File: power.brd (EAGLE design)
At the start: 90.2 x 95.9 mm, 19 parts, among them J1 POWER_JACKPTH_BREAD, U1 LT3652

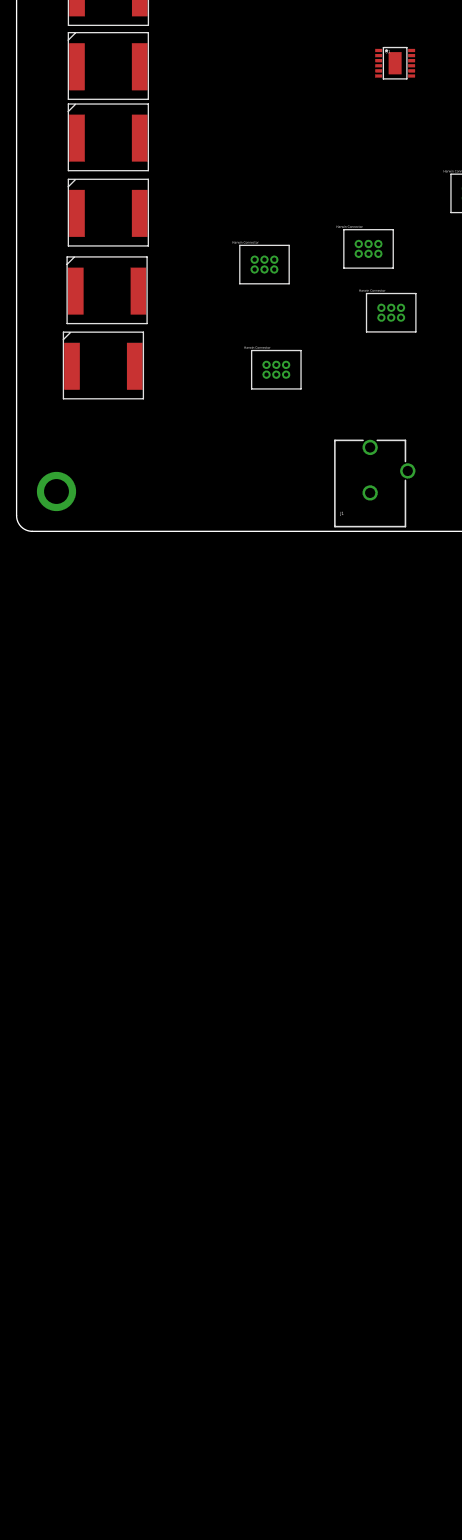
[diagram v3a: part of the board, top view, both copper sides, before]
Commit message: Added LT3688 dual regulator
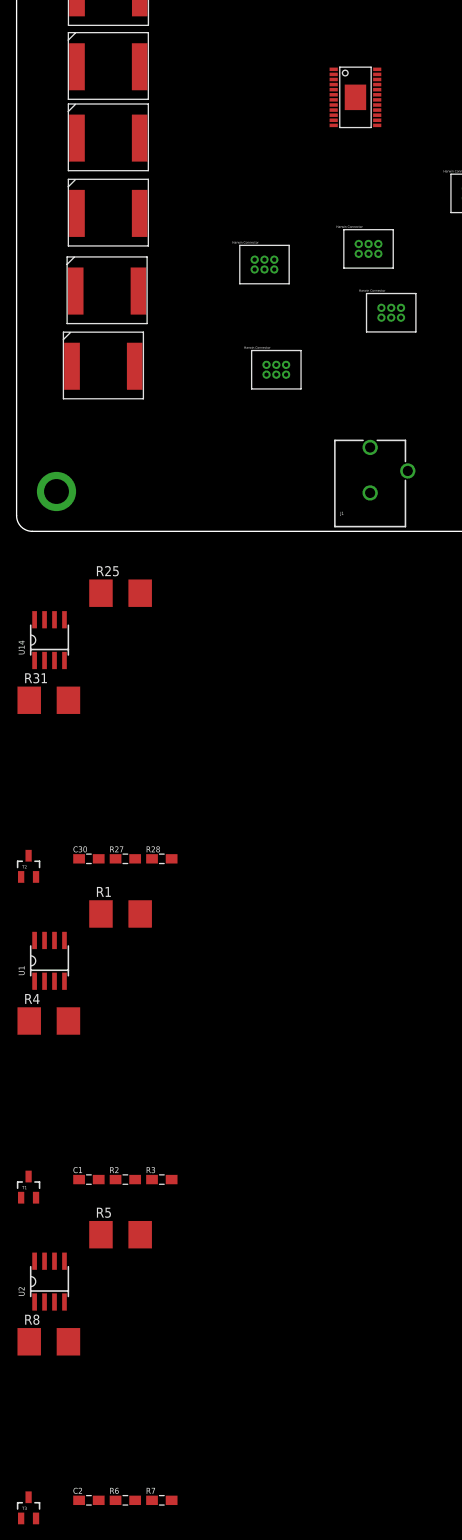
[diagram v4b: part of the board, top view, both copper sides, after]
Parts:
- added C1, C2, C30: .1uF, phonesat:0805
- added R1, R25, R31, R4, R5, R8: 0R, phonesat:2512
- added R2, R27, R6: 3K3, phonesat:0805
- added R28, R3, R7: 10K, phonesat:0805
- added T1, T2, T3: SINGLE_NCHAN_FET, phonesat:SOT23-3
- added U$13: LT3688, LT3688:LT3688TSSOP
- added U14, U2: MOSFET_PCHAN_20A, phonesat:SO8
- U1: value LT3652 -> MOSFET_PCHAN_20A; device SparkFun-PowerIC:MSOP-12_GND -> phonesat:SO8
- moved U1 122.7 mm to (4.20, -54.8)
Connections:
- new net ENAB_BURN1: R28.1, R3.1, R7.1
- new net N$1: R1.2, R4.2, U1.1, U1.2, U1.3
- new net N$19: R25.2, R31.2, U14.1, U14.2, U14.3
- new net N$2: C1.1, R3.2, T1.1
- new net N$21: C30.1, R28.2, T2.1
- new net N$24: R27.1, T2.3, U14.4
- new net N$3: R2.1, T1.3, U1.4
- new net N$4: R5.2, R8.2, U2.1, U2.2, U2.3
- new net N$5: C2.1, R7.2, T3.1
- new net N$6: R6.1, T3.3, U2.4
- new net VBURN1: U14.5, U14.6, U14.7, U14.8
- new net VBURN2: U1.5, U1.6, U1.7, U1.8
- new net VCC_8: R1.1, R2.2, R25.1, R27.2, R31.1, R4.1, R5.1, R6.2, R8.1
- new net VSOLAR: U$5.P3, U$5.P6
- net GND: now also C1.2, C2.2, C30.2, T1.2, T2.2, T3.2, U$1.P1, U$1.P4, U$2.P1, U$2.P4, U$3.P1, U$3.P4, U$4.P1, U$4.P4, U$5.P1, U$5.P4, U$6.P1, U$6.P4; no longer U1.13
- net VBURN3: now also U2.5, U2.6, U2.7, U2.8

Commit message: More switching regulator work
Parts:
- added C3, C4, C5: 0.22uF, SparkFun-Capacitors:0805
- added C31, C32: .1uF, phonesat:0805
- added C6, C7: 10pF, SparkFun-Capacitors:0805
- added C8, C9: 1nF, SparkFun-Capacitors:0805
- added R11: 523k, SparkFun-Resistors:0805
- added R12, R14: 100k, SparkFun-Resistors:0805
- added R13: 316k, SparkFun-Resistors:0805
- added R9: 10k, SparkFun-Resistors:0805
- C1: value .1uF -> 4.7uF; device phonesat:0805 -> SparkFun-Capacitors:0805
- C2: value .1uF -> 0.22uF; device phonesat:0805 -> SparkFun-Capacitors:0805
- moved C1 43.5 mm to (-1.42, -124.8)
- moved C2 16.6 mm to (-7.32, -124.8)
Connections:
- new net N$11: C3.1, U$13.BST2
- new net N$12: C6.2, R11.1, R12.2, U$13.FB1
- new net N$13: C8.2, U$13.RUNSS1
- new net N$14: C7.2, R13.1, R14.2, U$13.FB2
- new net N$7: R9.1, U$13.EN
- new net N$8: C9.1, U$13.RUNSS2
- new net N$9: C2.1, U$13.BST1
- net 3.3V: now also C3.2, C5.1, C7.1, R13.2, U$13.BIAS, U$13.SW2
- net 5V: now also C2.2, C4.1, C6.1, R11.2, U$13.SW1
- net GND: now also C31.2, C32.2, C4.2, C5.2, C8.1, C9.2, R12.1, R14.1, U$13.GND, U$13.WDE; no longer C2.2
- net N$2: now also C31.1; no longer C1.1
- net N$5: now also C32.1; no longer C2.1
- net VBATT: now also C1.1, R9.2, U$13.VIN

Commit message: Finished regulator circuit design
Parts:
- removed R1, R25, R31, R4, R5, R8: 0R, phonesat:2512
- added C10, C11: 4.7uF, SparkFun-Capacitors:0805
- added D1, D2: BAT20J, SparkFun-DiscreteSemi:SOD-323
- added L1, L2: SLF10145, SLF10145:SLF10145
- added R10: 110k, SparkFun-Resistors:0805
- C4, C5: value 0.22uF -> 22uF; device SparkFun-Capacitors:0805 -> SparkFun-Capacitors:1210
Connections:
- removed net N$1: R1.2, R4.2, U1.1, U1.2, U1.3
- removed net N$19: R25.2, R31.2, U14.1, U14.2, U14.3
- removed net N$4: R5.2, R8.2, U2.1, U2.2, U2.3
- removed net VCC_8: R1.1, R2.2, R25.1, R27.2, R31.1, R4.1, R5.1, R6.2, R8.1
- new net N$10: C2.2, D1.C, L1.P2, U$13.SW1
- new net N$15: C3.2, D2.C, L2.P1, U$13.SW2
- new net N$16: D1.A, U$13.DA1
- new net N$17: D2.A, U$13.DA2
- new net N$18: R10.2, U$13.RT
- new net N$20: C10.1, U$13.CPOR2
- new net N$22: C11.1, U$13.CPOR1
- net 3.3V: now also L2.P2; no longer C3.2, U$13.SW2
- net 5V: now also L1.P1, U$13.WDE; no longer C2.2, U$13.SW1
- net GND: now also C10.2, C11.2, R10.1, U$13.SYNC; no longer U$13.WDE
- net VBATT: now also R2.2, R27.2, R6.2, U1.1, U1.2, U1.3, U14.1, U14.2, U14.3, U2.1, U2.2, U2.3

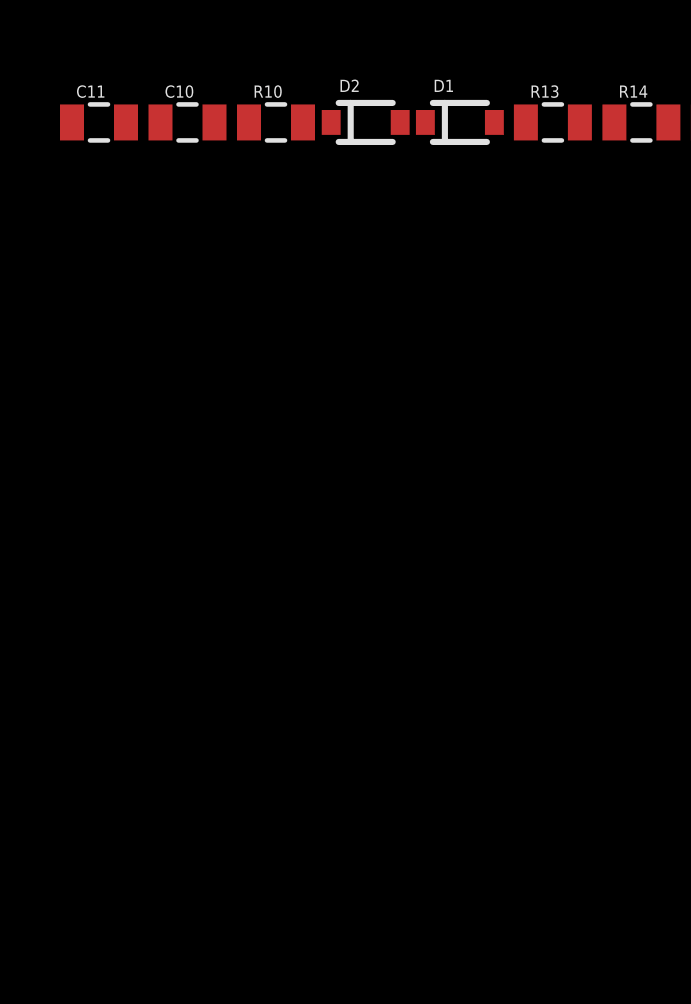
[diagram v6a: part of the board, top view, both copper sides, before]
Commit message: Added foot switch terminals to power board
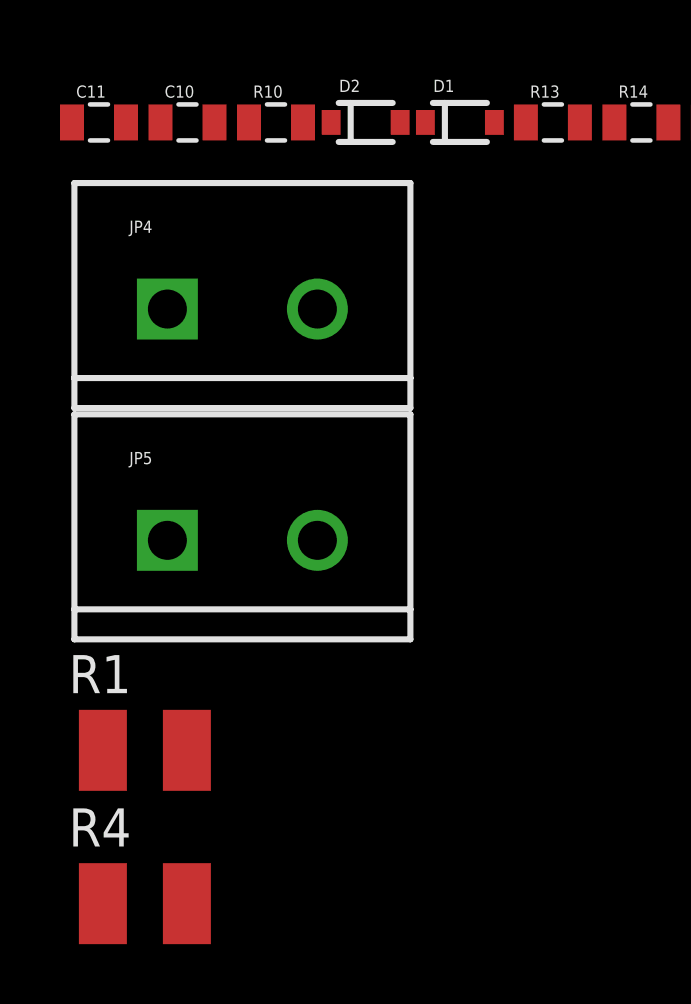
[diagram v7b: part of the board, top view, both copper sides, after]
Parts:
- added JP4, JP5: M025MM, SparkFun-Connectors:SCREWTERMINAL-5MM-2
- added R1, R4: 0R, rcl:R1210
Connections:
- new net BATT_INPUT: J1.PWR, JP1.2, JP2.2, JP4.2, R1.1
- new net ENAB_BURN2: R3.1
- new net ENAB_BURN3: R7.1
- new net N$4: JP4.1, JP5.2, R1.2, R4.1
- net ENAB_BURN1: no longer R3.1, R7.1
- net VBATT: now also JP5.1, R4.2; no longer J1.PWR, JP1.2, JP2.2
- net VBURN1: now also U$6.P2, U$6.P5
- net VBURN2: now also U$1.P2, U$1.P5
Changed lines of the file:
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@@
 <element name="C10" library="SparkFun-Capacitors" package="0805" value="4.7uF" x="-51.82" y="-124.81"/>
 <element name="C11" library="SparkFun-Capacitors" package="0805" value="4.7uF" x="-54.77" y="-124.81"/>
+<element name="JP4" library="SparkFun-Connectors" package="SCREWTERMINAL-5MM-2" value="M025MM" x="-52.49" y="-131.03"/>
+<element name="JP5" library="SparkFun-Connectors" package="SCREWTERMINAL-5MM-2" value="M025MM" x="-52.49" y="-138.74"/>
+<element name="R1" library="rcl" package="R1210" value="0R" x="-53.24" y="-145.74"/>
+<element name="R4" library="rcl" package="R1210" value="0R" x="-53.24" y="-150.85"/>
 </elements>
 <signals>
@@
 </signal>
 <signal name="VBATT">
-<contactref element="J1" pad="PWR"/>
-<contactref element="JP1" pad="2"/>
-<contactref element="JP2" pad="2"/>
 <contactref element="H2" pad="45"/>
 <contactref element="H2" pad="46"/>
@@
 <contactref element="U2" pad="1"/>
 <contactref element="U2" pad="3"/>
-<wire x1="69.85" y1="88.27" x2="69.85" y2="90.81" width="0" layer="19" extent="1-1"/>
-<wire x1="30.26" y1="72.44" x2="69.85" y2="88.27" width="0" layer="19" extent="1-1"/>
-<wire x1="40.435" y1="55.665" x2="30.26" y2="72.44" width="0" layer="19" extent="1-1"/>
-<wire x1="45.085" y1="10.7" x2="40.435" y2="55.665" width="0" layer="19" extent="1-1"/>
-<wire x1="80.98" y1="29.87" x2="45.085" y2="10.7" width="0" layer="19" extent="1-1"/>
-<wire x1="4.835" y1="-16.47" x2="45.085" y2="10.7" width="0" layer="19" extent="1-1"/>
+<contactref element="JP5" pad="1"/>
+<contactref element="R4" pad="2"/>
+<wire x1="-52.49" y1="-138.74" x2="-51.84" y2="-150.85" width="0" layer="19" extent="1-1"/>
+<wire x1="-3.47" y1="-124.81" x2="-52.49" y2="-138.74" width="0" layer="19" extent="1-1"/>
+<wire x1="-2.32" y1="-124.81" x2="-3.47" y2="-124.81" width="0" layer="19" extent="1-1"/>
+<wire x1="15.12" y1="-123.56" x2="-2.32" y2="-124.81" width="0" layer="19" extent="1-1"/>
+<wire x1="2.295" y1="-98.27" x2="-2.32" y2="-124.81" width="0" layer="19" extent="1-1"/>
+<wire x1="3.565" y1="-98.27" x2="2.295" y2="-98.27" width="0" layer="19" extent="1-1"/>
+<wire x1="4.835" y1="-98.27" x2="3.565" y2="-98.27" width="0" layer="19" extent="1-1"/>
+<wire x1="15.12" y1="-82.66" x2="4.835" y2="-98.27" width="0" layer="19" extent="1-1"/>
+<wire x1="4.835" y1="-57.37" x2="15.12" y2="-82.66" width="0" layer="19" extent="1-1"/>
+<wire x1="3.565" y1="-57.37" x2="4.835" y2="-57.37" width="0" layer="19" extent="1-1"/>
+<wire x1="2.295" y1="-57.37" x2="3.565" y2="-57.37" width="0" layer="19" extent="1-1"/>
+<wire x1="15.12" y1="-41.76" x2="4.835" y2="-57.37" width="0" layer="19" extent="1-1"/>
+<wire x1="4.835" y1="-16.47" x2="15.12" y2="-41.76" width="0" layer="19" extent="1-1"/>
 <wire x1="3.565" y1="-16.47" x2="4.835" y2="-16.47" width="0" layer="19" extent="1-1"/>
 <wire x1="2.295" y1="-16.47" x2="3.565" y2="-16.47" width="0" layer="19" extent="1-1"/>
-<wire x1="15.12" y1="-41.76" x2="4.835" y2="-16.47" width="0" layer="19" extent="1-1"/>
-<wire x1="4.835" y1="-57.37" x2="15.12" y2="-41.76" width="0" layer="19" extent="1-1"/>
-<wire x1="3.565" y1="-57.37" x2="4.835" y2="-57.37" width="0" layer="19" extent="1-1"/>
-<wire x1="2.295" y1="-57.37" x2="3.565" y2="-57.37" width="0" layer="19" extent="1-1"/>
-<wire x1="15.12" y1="-82.66" x2="4.835" y2="-57.37" width="0" layer="19" extent="1-1"/>
-<wire x1="4.835" y1="-98.27" x2="15.12" y2="-82.66" width="0" layer="19" extent="1-1"/>
-<wire x1="3.565" y1="-98.27" x2="4.835" y2="-98.27" width="0" layer="19" extent="1-1"/>
-<wire x1="2.295" y1="-98.27" x2="3.565" y2="-98.27" width="0" layer="19" extent="1-1"/>
-<wire x1="-2.32" y1="-124.81" x2="2.295" y2="-98.27" width="0" layer="19" extent="1-1"/>
-<wire x1="-3.47" y1="-124.81" x2="-2.32" y2="-124.81" width="0" layer="19" extent="1-1"/>
-<wire x1="15.12" y1="-123.56" x2="-2.32" y2="-124.81" width="0" layer="19" extent="1-1"/>
+<wire x1="40.435" y1="55.665" x2="4.835" y2="-16.47" width="0" layer="19" extent="1-1"/>
+<wire x1="69.85" y1="88.27" x2="40.435" y2="55.665" width="0" layer="19" extent="1-1"/>
+<wire x1="69.85" y1="90.81" x2="69.85" y2="88.27" width="0" layer="19" extent="1-1"/>
 </signal>
 <signal name="VBURN3">
@@
 <contactref element="U14" pad="5"/>
 <contactref element="U14" pad="6"/>
-<wire x1="3.565" y1="-11.27" x2="2.295" y2="-11.27" width="0" layer="19" extent="1-1"/>
-<wire x1="4.835" y1="-11.27" x2="3.565" y2="-11.27" width="0" layer="19" extent="1-1"/>
-<wire x1="6.105" y1="-11.27" x2="4.835" y2="-11.27" width="0" layer="19" extent="1-1"/>
+<contactref element="U$6" pad="P2"/>
+<contactref element="U$6" pad="P5"/>
+<wire x1="31.61" y1="33.39" x2="31.61" y2="34.64" width="0" layer="19" extent="1-1"/>
+<wire x1="6.105" y1="-11.27" x2="31.61" y2="33.39" width="0" layer="19" extent="1-1"/>
+<wire x1="4.835" y1="-11.27" x2="6.105" y2="-11.27" width="0" layer="19" extent="1-1"/>
+<wire x1="3.565" y1="-11.27" x2="4.835" y2="-11.27" width="0" layer="19" extent="1-1"/>
+<wire x1="2.295" y1="-11.27" x2="3.565" y2="-11.27" width="0" layer="19" extent="1-1"/>
 </signal>
 <signal name="N$21">
@@
 <signal name="ENAB_BURN1">
 <contactref element="R28" pad="1"/>
-<contactref element="R3" pad="1"/>
-<contactref element="R7" pad="1"/>
-<wire x1="17.27" y1="-82.66" x2="17.27" y2="-123.56" width="0" layer="19" extent="1-1"/>
-<wire x1="17.27" y1="-41.76" x2="17.27" y2="-82.66" width="0" layer="19" extent="1-1"/>
 </signal>
 <signal name="VBURN2">
@@
 <contactref element="U1" pad="5"/>
 <contactref element="U1" pad="6"/>
-<wire x1="3.565" y1="-52.17" x2="2.295" y2="-52.17" width="0" layer="19" extent="1-1"/>
-<wire x1="4.835" y1="-52.17" x2="3.565" y2="-52.17" width="0" layer="19" extent="1-1"/>
-<wire x1="6.105" y1="-52.17" x2="4.835" y2="-52.17" width="0" layer="19" extent="1-1"/>
+<contactref element="U$1" pad="P5"/>
+<contactref element="U$1" pad="P2"/>
+<wire x1="47.77" y1="27.25" x2="47.77" y2="28.5" width="0" layer="19" extent="1-1"/>
+<wire x1="6.105" y1="-52.17" x2="47.77" y2="27.25" width="0" layer="19" extent="1-1"/>
+<wire x1="4.835" y1="-52.17" x2="6.105" y2="-52.17" width="0" layer="19" extent="1-1"/>
+<wire x1="3.565" y1="-52.17" x2="4.835" y2="-52.17" width="0" layer="19" extent="1-1"/>
+<wire x1="2.295" y1="-52.17" x2="3.565" y2="-52.17" width="0" layer="19" extent="1-1"/>
 </signal>
 <signal name="N$2">
@@
 <wire x1="45.985" y1="56.315" x2="-55.67" y2="-124.81" width="0" layer="19" extent="1-1"/>
 </signal>
+<signal name="N$4">
+<contactref element="JP4" pad="1"/>
+<contactref element="JP5" pad="2"/>
+<contactref element="R1" pad="2"/>
+<contactref element="R4" pad="1"/>
+<wire x1="-51.84" y1="-145.74" x2="-54.64" y2="-150.85" width="0" layer="19" extent="1-1"/>
+<wire x1="-47.49" y1="-138.74" x2="-51.84" y2="-145.74" width="0" layer="19" extent="1-1"/>
+<wire x1="-52.49" y1="-131.03" x2="-47.49" y2="-138.74" width="0" layer="19" extent="1-1"/>
+</signal>
+<signal name="BATT_INPUT">
+<contactref element="JP1" pad="2"/>
+<contactref element="JP2" pad="2"/>
+<contactref element="JP4" pad="2"/>
+<contactref element="R1" pad="1"/>
+<contactref element="J1" pad="PWR"/>
+<wire x1="-47.49" y1="-131.03" x2="-54.64" y2="-145.74" width="0" layer="19" extent="1-1"/>
+<wire x1="45.085" y1="10.7" x2="-47.49" y2="-131.03" width="0" layer="19" extent="1-1"/>
+<wire x1="80.98" y1="29.87" x2="45.085" y2="10.7" width="0" layer="19" extent="1-1"/>
+<wire x1="30.26" y1="72.44" x2="45.085" y2="10.7" width="0" layer="19" extent="1-1"/>
+</signal>
+<signal name="ENAB_BURN2">
+<contactref element="R3" pad="1"/>
+</signal>
+<signal name="ENAB_BURN3">
+<contactref element="R7" pad="1"/>
+</signal>
 </signals>
